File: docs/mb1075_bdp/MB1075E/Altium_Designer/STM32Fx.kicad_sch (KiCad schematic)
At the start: 46 parts, among them U5 STM32F429ZIT6, X2 MC306-G-06Q-32.768, X3 8MHz

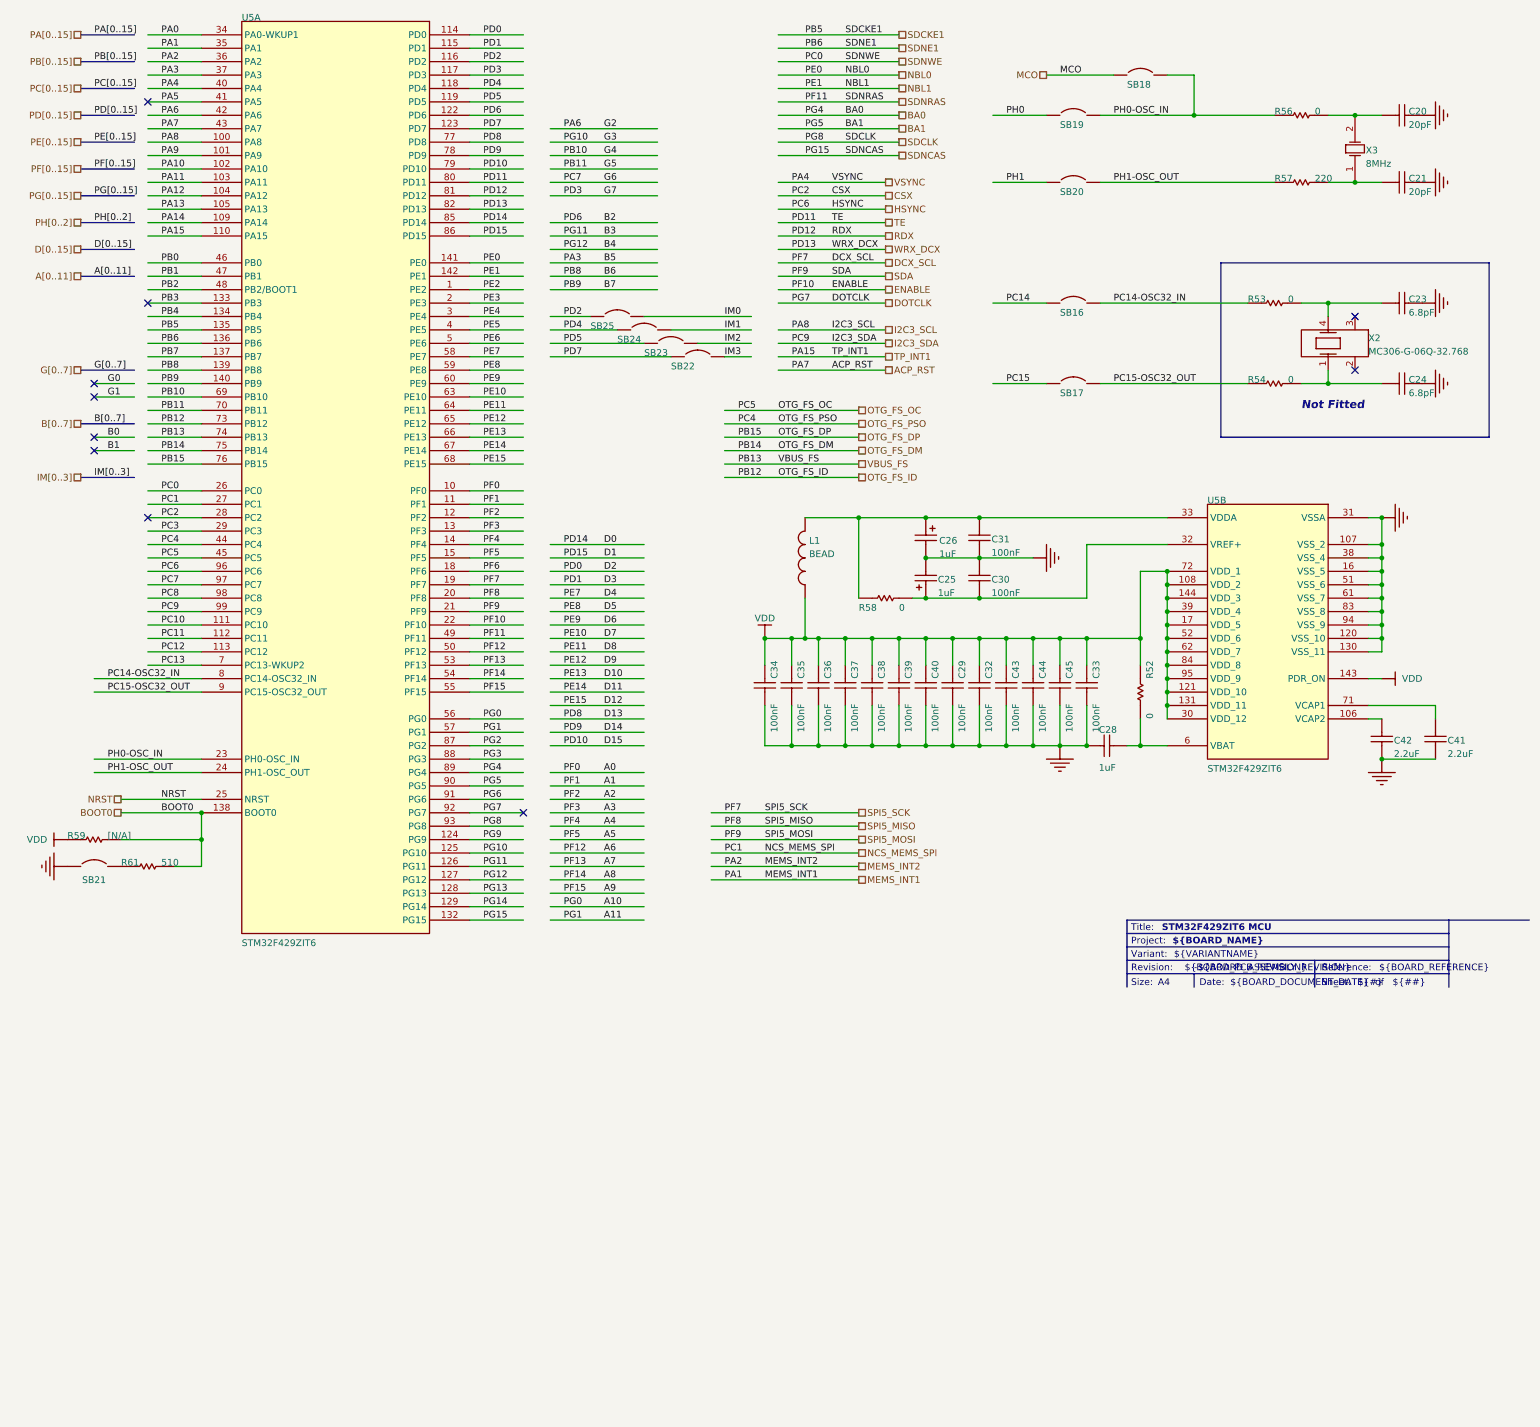
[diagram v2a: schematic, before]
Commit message: esd protection for usb data lines
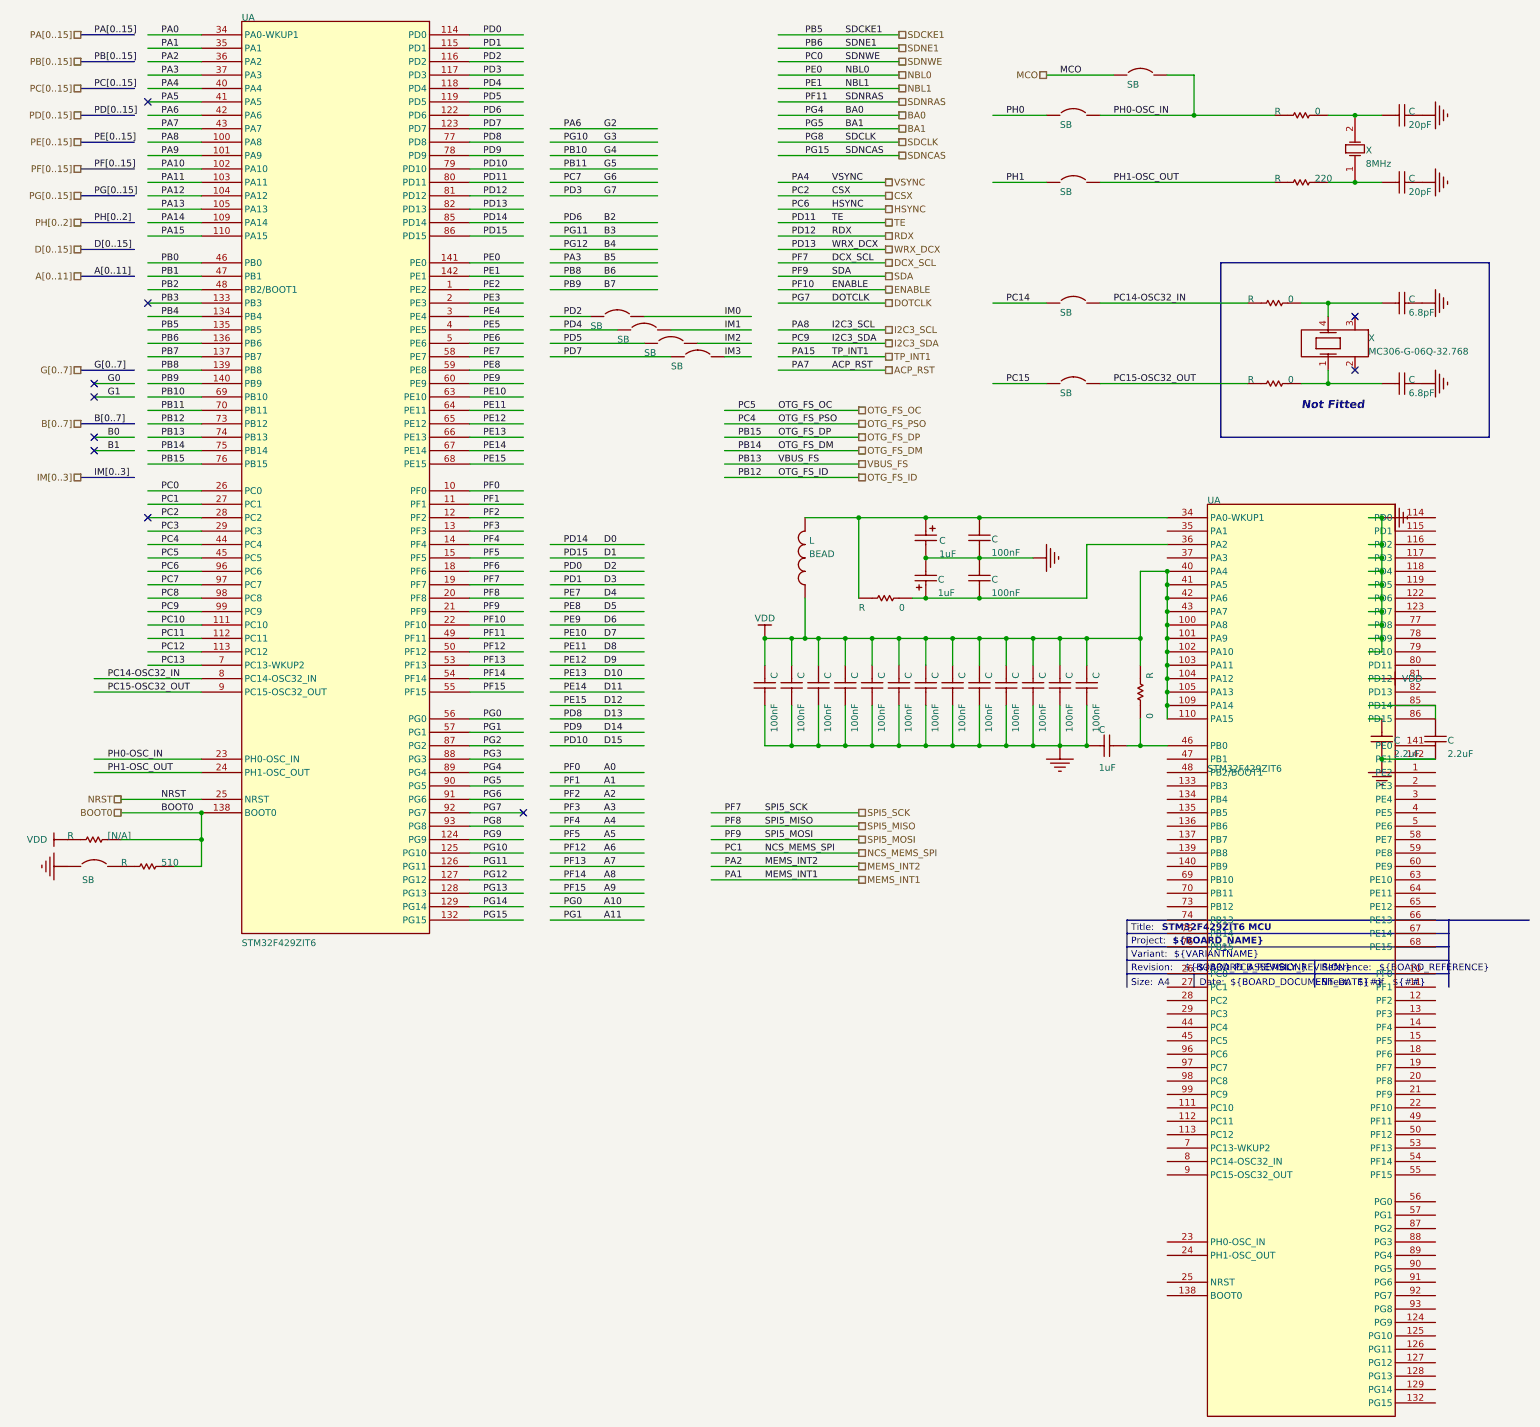
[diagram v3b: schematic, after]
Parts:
- removed C20, C21: 20pF, 0402C, symbol MCD_TOOLS:U_STM32Fx_0_Capacitor_ST_MCD_TOOLS.SchLib
- removed C23, C24: 6.8pF, 0402C, symbol MCD_TOOLS:U_STM32Fx_0_Capacitor_ST_MCD_TOOLS.SchLib
- removed C25: 1uF, TAN-A, symbol Miscellaneous Devices:U_STM32Fx_1_Cap Pol1_Miscellaneous Devices.IntLib
- removed C26: 1uF, TAN-A, symbol Miscellaneous Devices:U_STM32Fx_3_Cap Pol1_Miscellaneous Devices.IntLib
- removed C28: 1uF, 0603C, symbol MCD_TOOLS:U_STM32Fx_0_Capacitor_ST_MCD_TOOLS.SchLib
- removed C29, C30, C31, C32, C33, C34, C35, C36, C37, C38, C39, C40, C43, C44, C45: 100nF, 0402C, symbol MCD_TOOLS:U_STM32Fx_1_Capacitor_ST_MCD_TOOLS.SchLib
- removed C41, C42: 2.2uF, TAN-A, symbol MCD_TOOLS:U_STM32Fx_3_Cap Low ESR_MCD_TOOLS.SchLib
- removed L1: BEAD, 0603L, symbol MCD_TOOLS:U_STM32Fx_1_Inductor_MCD_TOOLS.SchLib
- removed R52: 0, 0402R, symbol MCD_TOOLS:U_STM32Fx_1_Resistor_ST_MCD_TOOLS.SchLib
- removed R53, R54, R56, R58: 0, 0402R, symbol MCD_TOOLS:U_STM32Fx_0_Resistor_ST_MCD_TOOLS.SchLib
- removed R57: 220, 0402R, symbol MCD_TOOLS:U_STM32Fx_0_Resistor_ST_MCD_TOOLS.SchLib
- removed R59: [N/A], 0402R, symbol MCD_TOOLS:U_STM32Fx_0_Resistor_ST_MCD_TOOLS.SchLib
- removed R61: 510, 0402R, symbol MCD_TOOLS:U_STM32Fx_0_Resistor_ST_MCD_TOOLS.SchLib
- removed SB16, SB17, SB18, SB19, SB20, SB21, SB22, SB23, SB24, SB25: Circuit Breaker, JP2_SMD, symbol MB915:U_STM32Fx_0_Circuit Breaker_MB915.SCHLIB
- removed U5: STM32F429ZIT6, TQFP144, symbol MCD_TOOLS:U_STM32Fx_0_STM32F429ZIT6U_MCD_TOOLS.SchLib
- removed X2: MC306-G-06Q-32.768, MC306-CRYSTAL, symbol MCD_TOOLS:U_STM32Fx_2_mirrored_XTAL_32K_MCD_TOOLS.SchLib
- removed X3: 8MHz, XTAL1, symbol MCD_TOOLS:U_STM32Fx_1_XTAL_MCD_TOOLS.SchLib_0
- added C (x15): 100nF, 0402C, symbol MCD_TOOLS:root_1_Capacitor_ST_MCD_TOOLS.SchLib
- added C: 1uF, TAN-A, symbol Miscellaneous Devices:root_3_Cap Pol1_Miscellaneous Devices.IntLib
- added C (x2): 20pF, 0402C, symbol MCD_TOOLS:root_0_Capacitor_ST_MCD_TOOLS.SchLib
- added C (x2): 2.2uF, TAN-A, symbol MCD_TOOLS:root_3_Cap Low ESR_MCD_TOOLS.SchLib
- added C: 1uF, 0603C, symbol MCD_TOOLS:root_0_Capacitor_ST_MCD_TOOLS.SchLib
- added C (x2): 6.8pF, 0402C, symbol MCD_TOOLS:root_0_Capacitor_ST_MCD_TOOLS.SchLib
- added C: 1uF, TAN-A, symbol Miscellaneous Devices:root_1_Cap Pol1_Miscellaneous Devices.IntLib
- added L: BEAD, 0603L, symbol MCD_TOOLS:root_1_Inductor_MCD_TOOLS.SchLib
- added R (x4): 0, 0402R, symbol MCD_TOOLS:root_0_Resistor_ST_MCD_TOOLS.SchLib
- added R: 510, 0402R, symbol MCD_TOOLS:root_0_Resistor_ST_MCD_TOOLS.SchLib
- added R: 0, 0402R, symbol MCD_TOOLS:root_1_Resistor_ST_MCD_TOOLS.SchLib
- added R: [N/A], 0402R, symbol MCD_TOOLS:root_0_Resistor_ST_MCD_TOOLS.SchLib
- added R: 220, 0402R, symbol MCD_TOOLS:root_0_Resistor_ST_MCD_TOOLS.SchLib
- added SB (x10): Circuit Breaker, JP2_SMD, symbol MB915:root_0_Circuit Breaker_MB915.SCHLIB
- added U (x2): STM32F429ZIT6, TQFP144, symbol MCD_TOOLS:root_0_STM32F429ZIT6U_MCD_TOOLS.SchLib
- added X: 8MHz, XTAL1, symbol MCD_TOOLS:root_1_XTAL_MCD_TOOLS.SchLib_0
- added X: MC306-G-06Q-32.768, MC306-CRYSTAL, symbol MCD_TOOLS:root_2_mirrored_XTAL_32K_MCD_TOOLS.SchLib
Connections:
- net A0: now also U.10 (PF0)
- net A1: now also U.11 (PF1)
- net A10: now also U.56 (PG0)
- net A11: now also U.57 (PG1)
- net A2: now also U.12 (PF2)
- net A3: now also U.13 (PF3)
- net A4: now also U.14 (PF4)
- net A5: now also U.15 (PF5)
- net A6: now also U.50 (PF12)
- net A7: now also U.53 (PF13)
- net A8: now also U.54 (PF14)
- net A9: now also U.55 (PF15)
- net ACP_RST: now also U.43 (PA7)
- net B2: now also U.122 (PD6)
- net B3: now also U.126 (PG11)
- net B4: now also U.127 (PG12)
- net B5: now also U.37 (PA3)
- net B6: now also U.139 (PB8)
- net B7: now also U.140 (PB9)
- net BA0: now also U.89 (PG4)
- net BA1: now also U.90 (PG5)
- net BOOT0: now also R.2, R.2, U.138 (BOOT0)
- net CSX: now also U.28 (PC2)
- net D0: now also U.85 (PD14)
- net D1: now also U.86 (PD15)
- net D10: now also U.66 (PE13)
- net D11: now also U.67 (PE14)
- net D12: now also U.68 (PE15)
- net D13: now also U.77 (PD8)
- net D14: now also U.78 (PD9)
- net D15: now also U.79 (PD10)
- net D2: now also U.114 (PD0)
- net D3: now also U.115 (PD1)
- net D4: now also U.58 (PE7)
- net D5: now also U.59 (PE8)
- net D6: now also U.60 (PE9)
- net D7: now also U.63 (PE10)
- net D8: now also U.64 (PE11)
- net D9: now also U.65 (PE12)
- net DCX_SCL: now also U.19 (PF7)
- net DOTCLK: now also U.92 (PG7)
- net ENABLE: now also U.22 (PF10)
- net G2: now also U.42 (PA6)
- net G3: now also U.125 (PG10)
- net G4: now also U.69 (PB10)
- net G5: now also U.70 (PB11)
- net G6: now also U.97 (PC7)
- net G7: now also U.117 (PD3)
- net GND: now also C.1, C.1, C.1, C.1, C.1, C.1, C.1, C.1, C.1, C.1, C.1, C.1, C.1, C.1, C.1, C.2, C.2, C.2, C.2, C.2, C.2, C.2, C.2, C.2, SB.1, U.142 (PE1)
- net HSYNC: now also U.96 (PC6)
- net I2C3_SCL: now also U.100 (PA8)
- net I2C3_SDA: now also U.99 (PC9)
- net IM0: now also SB.2
- net IM1: now also SB.2
- net IM2: now also SB.2
- net IM3: now also SB.2
- net MCO: now also SB.1
- net MEMS_INT1: now also U.35 (PA1)
- net MEMS_INT2: now also U.36 (PA2)
- net NBL0: now also U.141 (PE0)
- net NBL1: now also U.142 (PE1)
- net NCS_MEMS_SPI: now also U.27 (PC1)
- net NRST: now also U.25 (NRST)
- net OTG_FS_DM: now also U.75 (PB14)
- net OTG_FS_DP: now also U.76 (PB15)
- net OTG_FS_ID: now also U.73 (PB12)
- net OTG_FS_OC: now also U.45 (PC5)
- net OTG_FS_PSO: now also U.44 (PC4)
- net PA0: now also U.34 (PA0-WKUP1)
- net PA10: now also U.102 (PA10)
- net PA11: now also U.103 (PA11)
- net PA12: now also U.104 (PA12)
- net PA13: now also U.105 (PA13)
- net PA14: now also U.109 (PA14)
- net PA5: now also U.41 (PA5)
- net PA9: now also U.101 (PA9)
- net PB0: now also U.46 (PB0)
- net PB1: now also U.47 (PB1)
- net PB2: now also U.48 (PB2/BOOT1)
- net PB3: now also U.133 (PB3)
- net PB4: now also U.134 (PB4)
- net PB7: now also U.137 (PB7)
- net PC10: now also U.111 (PC10)
- net PC11: now also U.112 (PC11)
- net PC12: now also U.113 (PC12)
- net PC13: now also U.7 (PC13-WKUP2)
- net PC14: now also SB.1
- net PC14-OSC32_IN: now also R.1, SB.2, U.8 (PC14-OSC32_IN)
- net PC15: now also SB.1
- net PC15-OSC32_OUT: now also R.1, SB.2, U.9 (PC15-OSC32_OUT)
- net PC3: now also U.29 (PC3)
- net PC8: now also U.98 (PC8)
- net PD2: now also SB.1, U.116 (PD2)
- net PD4: now also SB.1, U.118 (PD4)
- net PD5: now also SB.1, U.119 (PD5)
- net PD7: now also SB.1, U.123 (PD7)
- net PE2: now also U.1 (PE2)
- net PE3: now also U.2 (PE3)
- net PE4: now also U.3 (PE4)
- net PE5: now also U.4 (PE5)
- net PE6: now also U.5 (PE6)
- net PF6: now also U.18 (PF6)
- net PG13: now also U.128 (PG13)
- net PG14: now also U.129 (PG14)
- net PG2: now also U.87 (PG2)
- net PG3: now also U.88 (PG3)
- net PG6: now also U.91 (PG6)
- net PG9: now also U.124 (PG9)
- net PH0: now also SB.1
- net PH0-OSC_IN: now also R.1, SB.2, SB.2, U.23 (PH0-OSC_IN)
- net PH1: now also SB.1
- net PH1-OSC_OUT: now also R.1, SB.2, U.24 (PH1-OSC_OUT)
- net RDX: now also U.81 (PD12)
- net SDA: now also U.21 (PF9)
- net SDCKE1: now also U.135 (PB5)
- net SDCLK: now also U.93 (PG8)
- net SDNCAS: now also U.132 (PG15)
- net SDNE1: now also U.136 (PB6)
- net SDNRAS: now also U.49 (PF11)
- net SDNWE: now also U.26 (PC0)
- net SPI5_MISO: now also U.20 (PF8)
- net TE: now also U.80 (PD11)
- net TP_INT1: now also U.110 (PA15)
- net VBUS_FS: now also U.74 (PB13)
- net VDD: now also C.2, C.2, C.2, C.2, C.2, C.2, C.2, C.2, C.2, C.2, C.2, C.2, C.2, L.1, R.1, R.2, U.100 (PA8), U.101 (PA9), U.102 (PA10), U.103 (PA11), U.104 (PA12), U.105 (PA13), U.109 (PA14), U.110 (PA15), U.40 (PA4), U.41 (PA5), U.42 (PA6), U.43 (PA7)
- net VSYNC: now also U.40 (PA4)
- net WRX_DCX: now also U.82 (PD13)
- new net: C.1, R.2, X.1 (OSC1)
- new net: C.1, R.2, X.2 (OSC2)
- new net: C.1, C.2, L.2, R.1, U.34 (PA0-WKUP1)
- new net: C.1, C.1, R.2, U.36 (PA2)
- new net: C.2, R.1, U.46 (PB0)
- new net: C.1, U.85 (PD14), U.86 (PD15)
- new net: R.1, SB.2
- new net: C.1, R.2, X.1
- new net: C.1, R.2, X.4

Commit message: measuring trace lengths, looks ok so far! almost done
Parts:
- removed C (x15): 100nF, 0402C, symbol MCD_TOOLS:root_1_Capacitor_ST_MCD_TOOLS.SchLib
- removed C (x2): 20pF, 0402C, symbol MCD_TOOLS:root_0_Capacitor_ST_MCD_TOOLS.SchLib
- removed C (x2): 2.2uF, TAN-A, symbol MCD_TOOLS:root_3_Cap Low ESR_MCD_TOOLS.SchLib
- removed C: 1uF, 0603C, symbol MCD_TOOLS:root_0_Capacitor_ST_MCD_TOOLS.SchLib
- removed C (x2): 6.8pF, 0402C, symbol MCD_TOOLS:root_0_Capacitor_ST_MCD_TOOLS.SchLib
- removed R (x4): 0, 0402R, symbol MCD_TOOLS:root_0_Resistor_ST_MCD_TOOLS.SchLib
- removed R: 510, 0402R, symbol MCD_TOOLS:root_0_Resistor_ST_MCD_TOOLS.SchLib
- removed R: [N/A], 0402R, symbol MCD_TOOLS:root_0_Resistor_ST_MCD_TOOLS.SchLib
- removed R: 220, 0402R, symbol MCD_TOOLS:root_0_Resistor_ST_MCD_TOOLS.SchLib
- removed SB (x10): Circuit Breaker, JP2_SMD, symbol MB915:root_0_Circuit Breaker_MB915.SCHLIB
- removed U (x2): STM32F429ZIT6, TQFP144, symbol MCD_TOOLS:root_0_STM32F429ZIT6U_MCD_TOOLS.SchLib
- added C (x15): 100nF, 0402C, symbol MCD_TOOLS:root_1_Capacitor_ST_MCD_TOOLS.SchLib
- added C: 1uF, 0603C, symbol MCD_TOOLS:root_0_Capacitor_ST_MCD_TOOLS.SchLib
- added C (x2): 20pF, 0402C, symbol MCD_TOOLS:root_0_Capacitor_ST_MCD_TOOLS.SchLib
- added C (x2): 2.2uF, TAN-A, symbol MCD_TOOLS:root_3_Cap Low ESR_MCD_TOOLS.SchLib
- added C (x2): 6.8pF, 0402C, symbol MCD_TOOLS:root_0_Capacitor_ST_MCD_TOOLS.SchLib
- added R (x4): 0, 0402R, symbol MCD_TOOLS:root_0_Resistor_ST_MCD_TOOLS.SchLib
- added R: [N/A], 0402R, symbol MCD_TOOLS:root_0_Resistor_ST_MCD_TOOLS.SchLib
- added R: 510, 0402R, symbol MCD_TOOLS:root_0_Resistor_ST_MCD_TOOLS.SchLib
- added R: 220, 0402R, symbol MCD_TOOLS:root_0_Resistor_ST_MCD_TOOLS.SchLib
- added SB (x10): Circuit Breaker, JP2_SMD, symbol MB915:root_0_Circuit Breaker_MB915.SCHLIB
- added U (x2): STM32F429ZIT6, TQFP144, symbol MCD_TOOLS:root_0_STM32F429ZIT6U_MCD_TOOLS.SchLib
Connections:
- net A0: now also U.10 (PF0)
- net A1: now also U.11 (PF1)
- net A10: now also U.56 (PG0)
- net A11: now also U.57 (PG1)
- net A2: now also U.12 (PF2)
- net A3: now also U.13 (PF3)
- net A4: now also U.14 (PF4)
- net A5: now also U.15 (PF5)
- net A6: now also U.50 (PF12)
- net A7: now also U.53 (PF13)
- net A8: now also U.54 (PF14)
- net A9: now also U.55 (PF15)
- net ACP_RST: now also U.43 (PA7)
- net B2: now also U.122 (PD6)
- net B3: now also U.126 (PG11)
- net B4: now also U.127 (PG12)
- net B5: now also U.37 (PA3)
- net B6: now also U.139 (PB8)
- net B7: now also U.140 (PB9)
- net BA0: now also U.89 (PG4)
- net BA1: now also U.90 (PG5)
- net BOOT0: now also R.2, R.2, U.138 (BOOT0)
- net CSX: now also U.28 (PC2)
- net D0: now also U.85 (PD14)
- net D1: now also U.86 (PD15)
- net D10: now also U.66 (PE13)
- net D11: now also U.67 (PE14)
- net D12: now also U.68 (PE15)
- net D13: now also U.77 (PD8)
- net D14: now also U.78 (PD9)
- net D15: now also U.79 (PD10)
- net D2: now also U.114 (PD0)
- net D3: now also U.115 (PD1)
- net D4: now also U.58 (PE7)
- net D5: now also U.59 (PE8)
- net D6: now also U.60 (PE9)
- net D7: now also U.63 (PE10)
- net D8: now also U.64 (PE11)
- net D9: now also U.65 (PE12)
- net DCX_SCL: now also U.19 (PF7)
- net DOTCLK: now also U.92 (PG7)
- net ENABLE: now also U.22 (PF10)
- net G2: now also U.42 (PA6)
- net G3: now also U.125 (PG10)
- net G4: now also U.69 (PB10)
- net G5: now also U.70 (PB11)
- net G6: now also U.97 (PC7)
- net G7: now also U.117 (PD3)
- net GND: now also C.1, C.1, C.1, C.1, C.1, C.1, C.1, C.1, C.1, C.1, C.1, C.1, C.1, C.1, C.1, C.2, C.2, C.2, C.2, C.2, C.2, C.2, SB.1, U.142 (PE1)
- net HSYNC: now also U.96 (PC6)
- net I2C3_SCL: now also U.100 (PA8)
- net I2C3_SDA: now also U.99 (PC9)
- net IM0: now also SB.2
- net IM1: now also SB.2
- net IM2: now also SB.2
- net IM3: now also SB.2
- net MCO: now also SB.1
- net MEMS_INT1: now also U.35 (PA1)
- net MEMS_INT2: now also U.36 (PA2)
- net NBL0: now also U.141 (PE0)
- net NBL1: now also U.142 (PE1)
- net NCS_MEMS_SPI: now also U.27 (PC1)
- net NRST: now also U.25 (NRST)
- net OTG_FS_DM: now also U.75 (PB14)
- net OTG_FS_DP: now also U.76 (PB15)
- net OTG_FS_ID: now also U.73 (PB12)
- net OTG_FS_OC: now also U.45 (PC5)
- net OTG_FS_PSO: now also U.44 (PC4)
- net PA0: now also U.34 (PA0-WKUP1)
- net PA10: now also U.102 (PA10)
- net PA11: now also U.103 (PA11)
- net PA12: now also U.104 (PA12)
- net PA13: now also U.105 (PA13)
- net PA14: now also U.109 (PA14)
- net PA5: now also U.41 (PA5)
- net PA9: now also U.101 (PA9)
- net PB0: now also U.46 (PB0)
- net PB1: now also U.47 (PB1)
- net PB2: now also U.48 (PB2/BOOT1)
- net PB3: now also U.133 (PB3)
- net PB4: now also U.134 (PB4)
- net PB7: now also U.137 (PB7)
- net PC10: now also U.111 (PC10)
- net PC11: now also U.112 (PC11)
- net PC12: now also U.113 (PC12)
- net PC13: now also U.7 (PC13-WKUP2)
- net PC14: now also SB.1
- net PC14-OSC32_IN: now also R.1, SB.2, U.8 (PC14-OSC32_IN)
- net PC15: now also SB.1
- net PC15-OSC32_OUT: now also R.1, SB.2, U.9 (PC15-OSC32_OUT)
- net PC3: now also U.29 (PC3)
- net PC8: now also U.98 (PC8)
- net PD2: now also SB.1, U.116 (PD2)
- net PD4: now also SB.1, U.118 (PD4)
- net PD5: now also SB.1, U.119 (PD5)
- net PD7: now also SB.1, U.123 (PD7)
- net PE2: now also U.1 (PE2)
- net PE3: now also U.2 (PE3)
- net PE4: now also U.3 (PE4)
- net PE5: now also U.4 (PE5)
- net PE6: now also U.5 (PE6)
- net PF6: now also U.18 (PF6)
- net PG13: now also U.128 (PG13)
- net PG14: now also U.129 (PG14)
- net PG2: now also U.87 (PG2)
- net PG3: now also U.88 (PG3)
- net PG6: now also U.91 (PG6)
- net PG9: now also U.124 (PG9)
- net PH0: now also SB.1
- net PH0-OSC_IN: now also R.1, SB.2, SB.2, U.23 (PH0-OSC_IN)
- net PH1: now also SB.1
- net PH1-OSC_OUT: now also R.1, SB.2, U.24 (PH1-OSC_OUT)
- net RDX: now also U.81 (PD12)
- net SDA: now also U.21 (PF9)
- net SDCKE1: now also U.135 (PB5)
- net SDCLK: now also U.93 (PG8)
- net SDNCAS: now also U.132 (PG15)
- net SDNE1: now also U.136 (PB6)
- net SDNRAS: now also U.49 (PF11)
- net SDNWE: now also U.26 (PC0)
- net SPI5_MISO: now also U.20 (PF8)
- net TE: now also U.80 (PD11)
- net TP_INT1: now also U.110 (PA15)
- net VBUS_FS: now also U.74 (PB13)
- net VDD: now also C.2, C.2, C.2, C.2, C.2, C.2, C.2, C.2, C.2, C.2, C.2, C.2, C.2, R.1, U.100 (PA8), U.101 (PA9), U.102 (PA10), U.103 (PA11), U.104 (PA12), U.105 (PA13), U.109 (PA14), U.110 (PA15), U.40 (PA4), U.41 (PA5), U.42 (PA6), U.43 (PA7)
- net VSYNC: now also U.40 (PA4)
- net WRX_DCX: now also U.82 (PD13)
- net at X.1 (OSC1): now also C.1, R.2
- net at X.2 (OSC2): now also C.1, R.2
- net at C.1, L.2: now also C.2, R.1, U.34 (PA0-WKUP1)
- net at C.1: now also C.1, R.2, U.36 (PA2)
- net at R.1: now also C.2, U.46 (PB0)
- net at X.1: now also C.1, R.2
- net at X.4: now also C.1, R.2
- new net: C.1, U.85 (PD14), U.86 (PD15)
- new net: R.1, SB.2
